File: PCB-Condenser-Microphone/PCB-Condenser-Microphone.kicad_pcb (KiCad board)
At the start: 2 copper layers, 21 parts, among them J1 Conn_01x02, J2 SJ-3523-SMT, SW1 SW_SPDT, U1 LM358

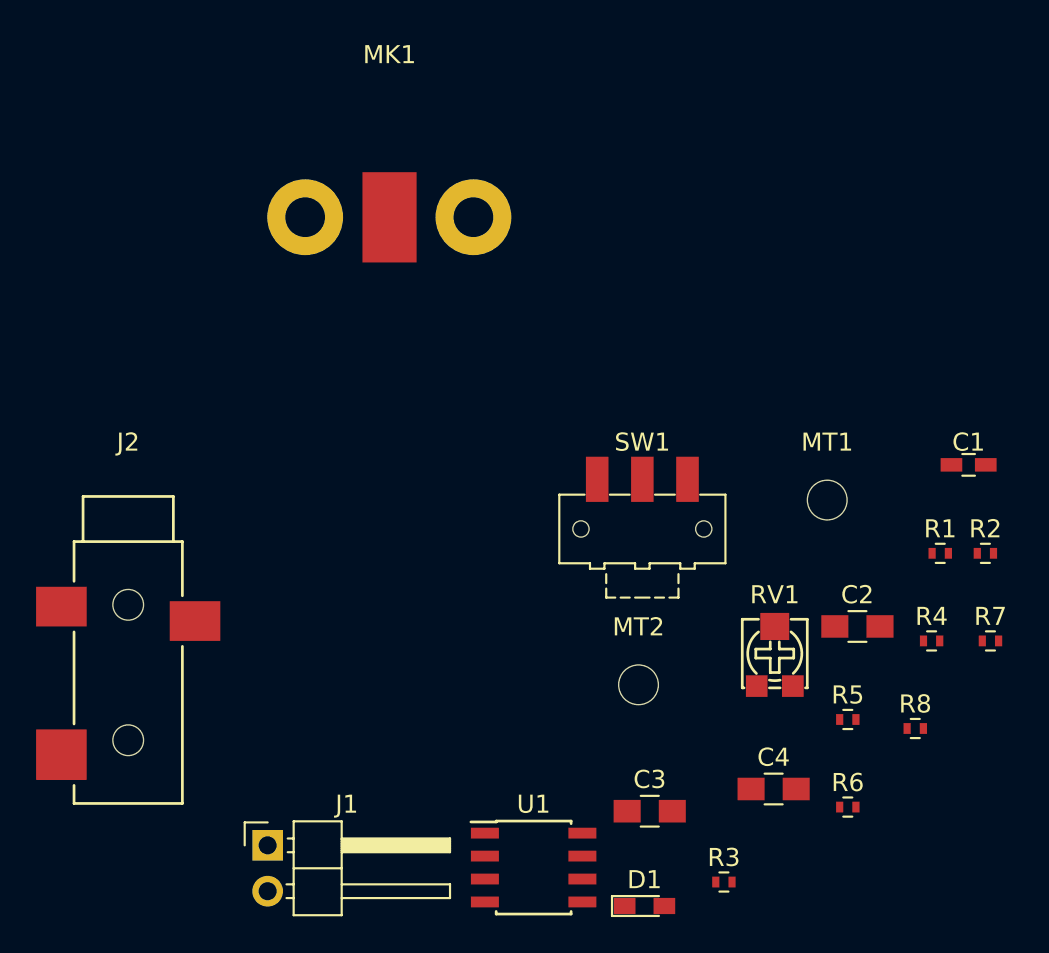
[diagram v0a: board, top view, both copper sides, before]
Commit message: Layd out pcb and added OSHW logo
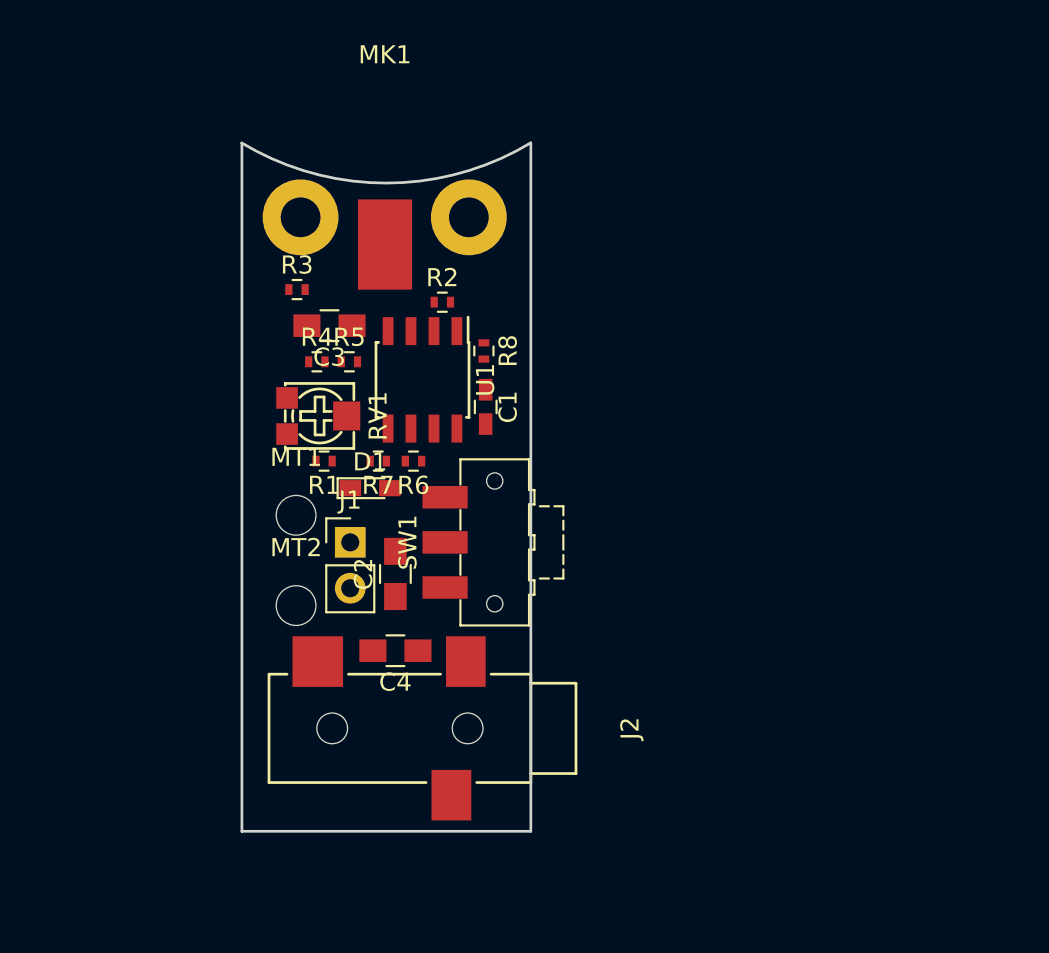
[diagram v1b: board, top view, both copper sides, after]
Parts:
- added REF***: OSHW-Logo_5.7x6mm_SilkScreen, Symbols:OSHW-Logo_5.7x6mm_SilkScreen, B.Cu at (126.7, 81.0)
- J1: footprint Pin_Headers:Pin_Header_Angled_1x02_Pitch2.54mm -> Pin_Headers:Pin_Header_Straight_1x02_Pitch2.54mm
- moved R3 40.4 mm to (121.0, 55.0)
- moved R4 37.4 mm to (122.2, 59.0)
- moved R7 35.3 mm to (125.5, 64.5), turned to 180 degrees
- moved R1 34.5 mm to (122.5, 64.5), turned to 180 degrees
- moved R5 34.0 mm to (124.0, 59.0)
- moved R2 33.1 mm to (129.1, 55.7)
- moved C3 32.2 mm to (122.8, 57.0), turned to 180 degrees
- moved R8 31.7 mm to (131.4, 58.4), turned to 270 degrees
- moved R6 30.7 mm to (127.5, 64.5), turned to 180 degrees
- moved MT1 29.4 mm to (121.0, 67.5)
- moved RV1 28.4 mm to (122.3, 62.0), turned to 270 degrees
- moved U1 27.7 mm to (128.0, 60.0), turned to 270 degrees
- moved D1 27.7 mm to (125.1, 66.0)
- moved C1 26.9 mm to (131.5, 61.5), turned to 270 degrees
- moved C2 25.7 mm to (126.5, 70.8), turned to 90 degrees
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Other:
- board outline added: 16 x 38.1 mm

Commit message: Routed PCB
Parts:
- moved REF*** 22.5 mm to (121.5, 59.2), turned to 90 degrees
- moved J1 2.50 mm to (124.0, 71.5), turned to 180 degrees
- moved R8 1.90 mm to (131.4, 56.5), turned to 90 degrees
- moved R4 0.52 mm to (122.0, 58.5)
- moved R5 0.52 mm to (123.8, 58.5)
- turned R2 to 180 degrees
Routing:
- net +9V: track 0.00 -> 57.4 mm
- net Net-(C4-Pad2): track 0.00 -> 24.9 mm
- net Net-(C3-Pad2): track 0.00 -> 20.9 mm
- net GND: track 0.00 -> 16.7 mm, vias 0 -> 10
- net Net-(R8-Pad1): track 0.00 -> 14.1 mm
- net Net-(J1-Pad2): track 0.00 -> 6.06 mm
- net Net-(C3-Pad1): track 0.00 -> 5.09 mm
- net Net-(RV1-Pad2): track 0.00 -> 4.46 mm
- net Net-(R2-Pad1): track 0.00 -> 3.97 mm
- net Net-(C4-Pad1): track 0.00 -> 2.90 mm
- net Net-(R6-Pad2): track 0.00 -> 2.89 mm
- net Net-(D1-Pad1): track 0.00 -> 1.91 mm
- net Net-(R4-Pad2): track 0.00 -> 0.90 mm
- added copper zone on B.Cu, net GND
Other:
- rule pad_to_mask_clearance: 0.2 -> 0
- board text added: "9V"
- board text added: "GND"
- board text added: "PCB Condenser Microphone - Rev 1 (c) 2018 Corwin Hansen corwinh.com"
